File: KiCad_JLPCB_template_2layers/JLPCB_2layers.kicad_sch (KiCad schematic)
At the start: 64 parts, among them J1 NS Connector, J2 EW Connector, J3 Control Logic Connector, J4 +5V, SW1 RST, SW2 OVR, SW3 EN, U1 SM420561N, U2 SM420561N, U3 LM1117DT-3.3

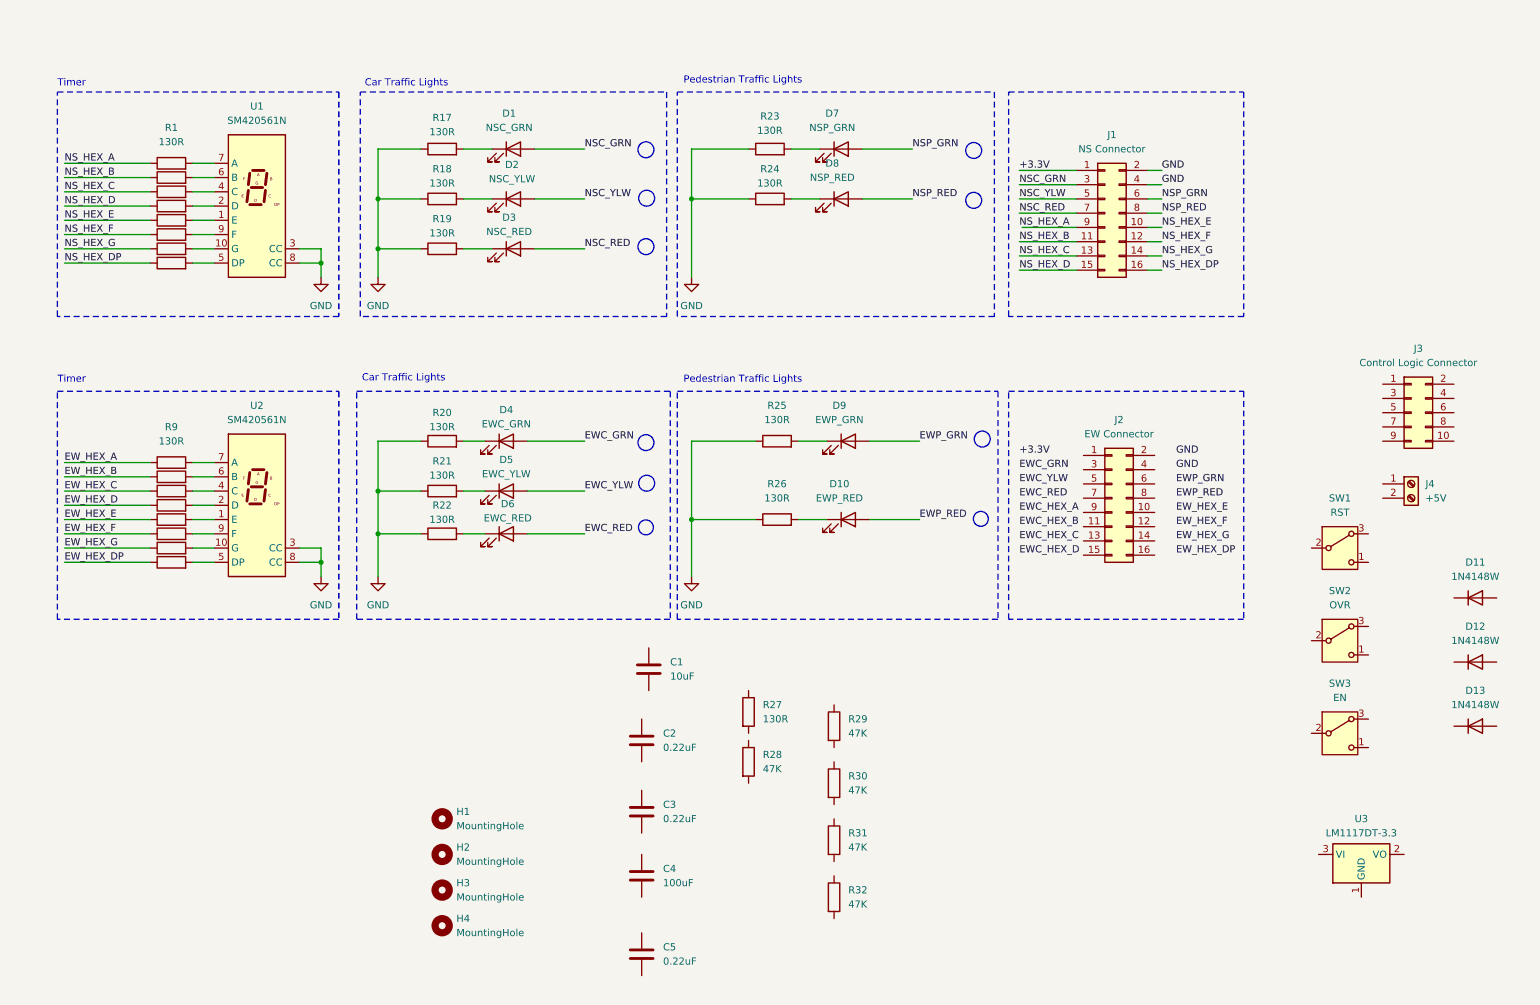
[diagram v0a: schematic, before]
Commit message: Finalize Traffic Light Schematics
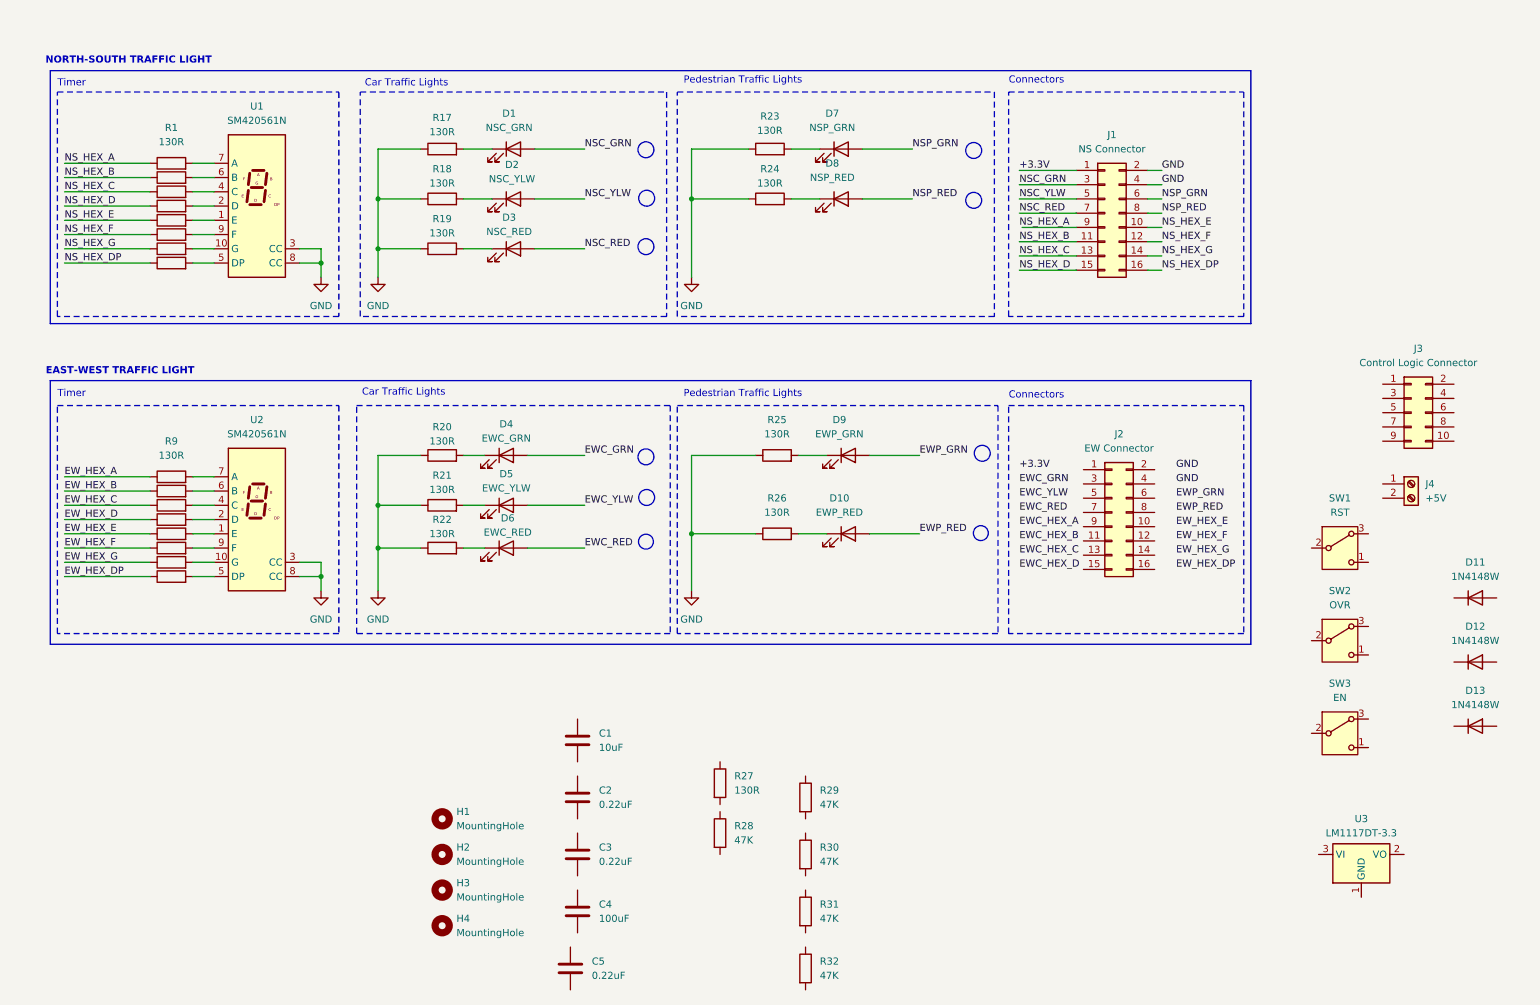
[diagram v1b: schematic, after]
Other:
- note added: "Connectors"
- note added: "EAST-WEST TRAFFIC LIGHT"
- note added: "NORTH-SOUTH TRAFFIC LIGHT"
- moved on the sheet: C1, C2, C3, C4, C5, D10, D4, D5, D6, D9, J2, R20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

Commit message: Finalized Schematic Diagram
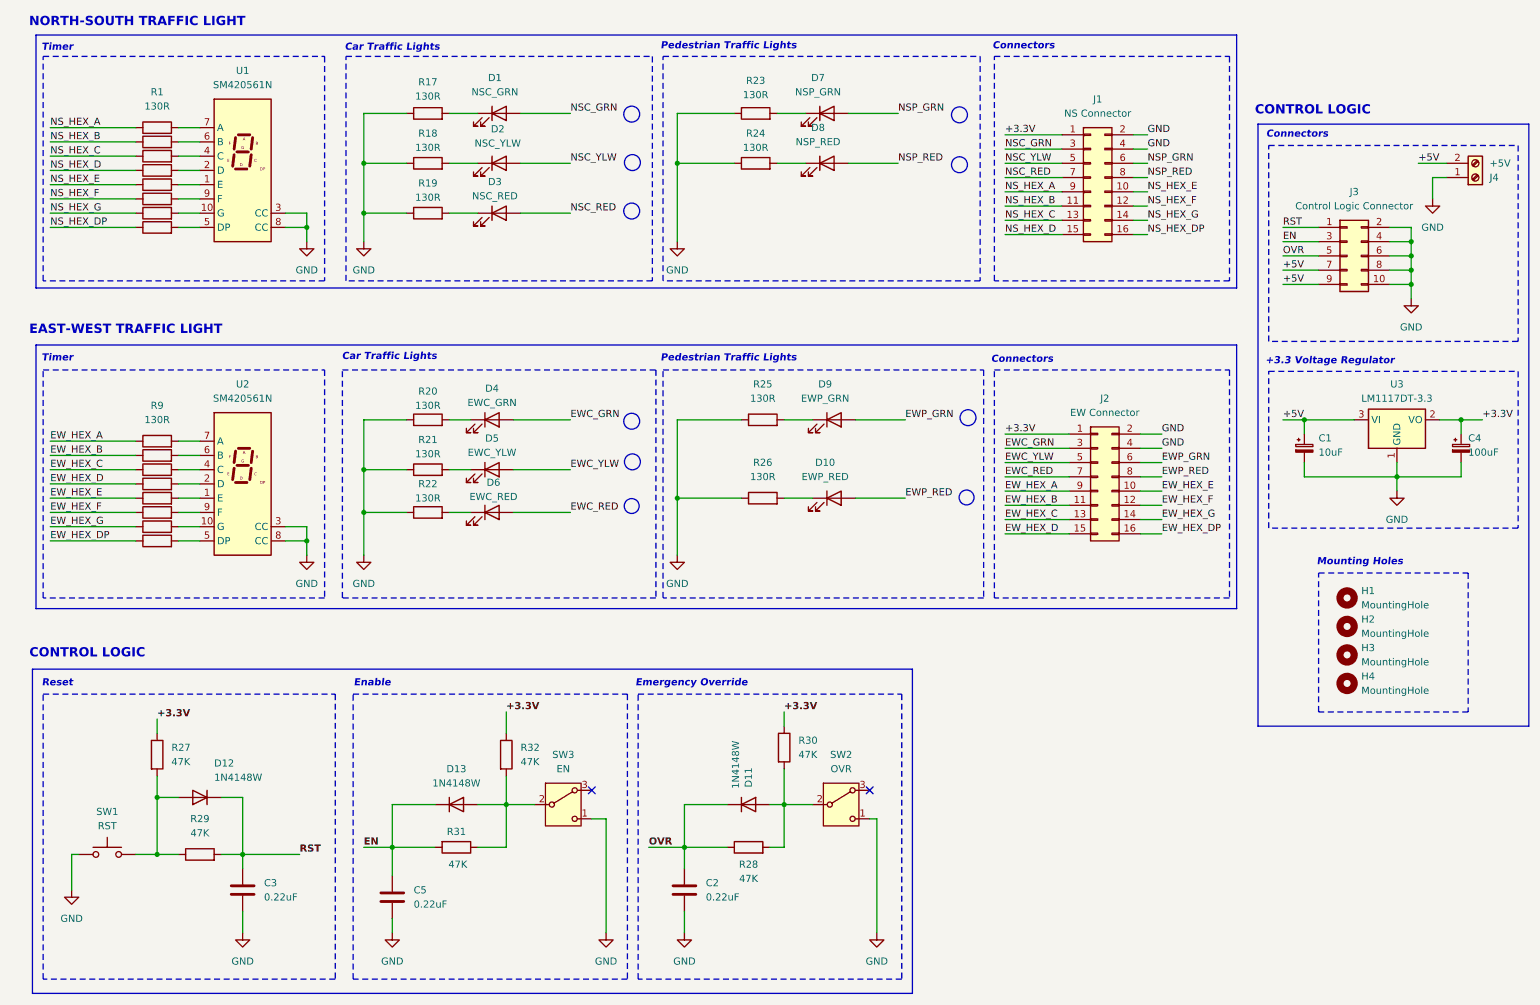
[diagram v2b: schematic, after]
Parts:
- removed C1: 10uF, Capacitor_SMD:CP_Elec_4x5.3, symbol Device:C
- removed C4: 100uF, Capacitor_SMD:CP_Elec_6.3x5.8, symbol Device:C
- removed SW1: RST, my_footprints:tact_switch_5mm, symbol Switch:SW_Nidec_CAS-120A1
- added C1: 10uF, Capacitor_SMD:CP_Elec_4x5.3, symbol Device:C_Polarized_Small
- added C4: 100uF, Capacitor_SMD:CP_Elec_6.3x5.8, symbol Device:C_Polarized_Small
- added SW1: RST, my_footprints:tact_switch_5mm, symbol Switch:SW_MEC_5G
- C5: footprint LED_THT:LED_D5.0mm -> Capacitor_SMD:C_1206_3216Metric_Pad1.33x1.80mm_HandSolder
- D1, D10, D2, D3, D4, D5, D6, D7, D8, D9: footprint (none) -> LED_THT:LED_D5.0mm
- J1, J2, J3: footprint (none) -> Connector_PinHeader_2.54mm:PinHeader_2x08_P2.54mm_Vertical
- J4: footprint (none) -> my_footprints:Terminal_Block_5mm
- R27: value 130R -> 47K
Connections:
- net +3.3V: now also J2.1 (Pin_1), R27.1, R30.1, R32.1, U3.2 (VO), C4.1
- net EWC_GRN: now also J2.3 (Pin_3)
- net EWC_RED: now also J2.7 (Pin_7)
- net EWC_YLW: now also J2.5 (Pin_5)
- net EWP_GRN: now also J2.6 (Pin_6)
- net EWP_RED: now also J2.8 (Pin_8)
- net EW_HEX_A: now also J2.9 (Pin_9)
- net EW_HEX_B: now also J2.11 (Pin_11)
- net EW_HEX_C: now also J2.13 (Pin_13)
- net EW_HEX_D: now also J2.15 (Pin_15)
- net EW_HEX_DP: now also J2.16 (Pin_16)
- net EW_HEX_E: now also J2.10 (Pin_10)
- net EW_HEX_F: now also J2.12 (Pin_12)
- net EW_HEX_G: now also J2.14 (Pin_14)
- net GND: now also C2.2, C3.2, C5.2, J2.2 (Pin_2), J2.4 (Pin_4), J3.10 (Pin_10), J3.2 (Pin_2), J3.4 (Pin_4), J3.6 (Pin_6), J3.8 (Pin_8), J4.1 (Pin_1), SW2.1 (C), SW3.1 (C), U3.1 (GND), C1.2, C4.2, SW1.1 (A), SW1.2 (A)
- net NS_HEX_A: now also J1.9 (Pin_9)
- net RST: now reaches J3.1 (Pin_1)
- net RST: now also C3.1, D12.1 (K), R29.2
- net EN: now reaches J3.3 (Pin_3)
- net EN: now also C5.1, D13.1 (K), R31.2
- net OVR: now reaches J3.5 (Pin_5)
- net OVR: now also C2.1, D11.1 (K), R28.1
- net +5V: now reaches J3.7 (Pin_7)
- net +5V: now also J3.9 (Pin_9), J4.2 (Pin_2), U3.3 (VI), C1.1
- net at SW2.2 (B): now also D11.2 (A), R28.2, R30.2
- net at D12.2 (A): now also R27.2, R29.1, SW1.3 (B), SW1.4 (B)
- net at R31.1: now also D13.2 (A), R32.2, SW3.2 (B)
- no-connect marks 0 -> 2
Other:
- note added: "+3.3 Voltage Regulator"
- note added: "CONTROL LOGIC"
- note added: "Emergency Override"
- note added: "Enable"
- note added: "Mounting Holes"
- note added: "Reset"
- moved on the sheet: C2, C3, C5, D1, D10, D11, D12, D13, D2, D3, D4, D5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

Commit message: Starting up PCB
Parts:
- J3: footprint Connector_PinHeader_2.54mm:PinHeader_2x08_P2.54mm_Vertical -> Connector_PinHeader_2.54mm:PinHeader_2x05_P2.54mm_Vertical
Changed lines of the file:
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@@
 			)
 		)
-		(property "Footprint" "Connector_PinHeader_2.54mm:PinHeader_2x08_P2.54mm_Vertical"
+		(property "Footprint" "Connector_PinHeader_2.54mm:PinHeader_2x05_P2.54mm_Vertical"
 			(at 250.19 60.96 0)
 			(effects
